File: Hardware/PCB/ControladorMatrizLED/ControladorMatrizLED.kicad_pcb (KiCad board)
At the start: 2 copper layers, 18 parts

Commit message: Avance sobre Esquematico y PCB - Pistas terminadas
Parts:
- moved C2_OUT1 51.8 mm to (135.6, 78.2), turned to 270 degrees
- moved C1_OUT1 47.2 mm to (112.3, 124.5), turned to 90 degrees
- moved C3_OUT1 27.7 mm to (108.0, 78.2)
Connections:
- C1_OUT1 pad 1: /C1_QA -> C1_QA
- C1_OUT1 pad 2: /C1_QB -> C1_QB
- C1_OUT1 pad 3: /C1_QC -> C1_QC
- C1_OUT1 pad 4: /C1_QD -> C1_QD
- C1_OUT1 pad 5: /C1_QE -> C1_QE
- C1_OUT1 pad 6: /C1_QF -> C1_QF
- C1_OUT1 pad 7: /C1_QG -> C1_QG
- C1_OUT1 pad 8: /C1_QH -> C1_QH
- C2_OUT1 pad 1: /C2_QA -> C2_QA
- C2_OUT1 pad 2: /C2_QB -> C2_QB
- C2_OUT1 pad 3: /C2_QC -> C2_QC
- C2_OUT1 pad 4: /C2_QD -> C2_QD
- C2_OUT1 pad 5: /C2_QE -> C2_QE
- C2_OUT1 pad 6: /C2_QF -> C2_QF
- C2_OUT1 pad 7: /C2_QG -> C2_QG
- C2_OUT1 pad 8: /C2_QH -> C2_QH
- C3_OUT1 pad 1: /C3_QA -> C3_QA
- C3_OUT1 pad 2: /C3_QB -> C3_QB
- C3_OUT1 pad 3: /C3_QC -> C3_QC
- C3_OUT1 pad 4: /C3_QD -> C3_QD
- C3_OUT1 pad 5: /C3_QE -> C3_QE
- C3_OUT1 pad 6: /C3_QF -> C3_QF
- C3_OUT1 pad 7: /C3_QG -> C3_QG
- C3_OUT1 pad 8: /C3_QH -> C3_QH
- EXP_C1 pad 1: /C3_SD -> C3_SD
- EXP_C1 pad 2: /C3_CLK -> C3_CLK
- EXP_C1 pad 3: /C3_LATCH -> C3_LATCH
- EXP_F1 pad 1: /F1_SD -> F1_SD
- EXP_F1 pad 2: /F1_CLK -> F1_CLK
- EXP_F1 pad 3: /F1_LATCH -> C3_LATCH
- F1_OUT1 pad 1: /F1_QA -> F1_QA
- F1_OUT1 pad 2: /F1_QB -> F1_QB
- F1_OUT1 pad 3: /F1_QC -> F1_QC
- F1_OUT1 pad 4: /F1_QD -> F1_QD
- F1_OUT1 pad 5: /F1_QE -> F1_QE
- F1_OUT1 pad 6: /F1_QF -> F1_QF
- F1_OUT1 pad 7: /F1_QG -> F1_QG
- F1_OUT1 pad 8: /F1_QH -> F1_QH
- J_MODE_CLK1 pad 1: /CMLED/GPIO3 -> F1_CLK
- J_MODE_CLK1 pad 3: /CMLED/GPIO8 -> C3_CLK
- J_MODE_SD1 pad 1: /CMLED/JF_OUT -> F1_SD
- REGC1 pad 1: /CMLED/C1_QB -> C1_QB
- REGC1 pad 11: /CMLED/GPIO8 -> C3_CLK
- REGC1 pad 12: /CMLED/GPIO5 -> C3_LATCH
- REGC1 pad 15: /CMLED/C1_QA -> C1_QA
- REGC1 pad 2: /CMLED/C1_QC -> C1_QC
- REGC1 pad 3: /CMLED/C1_QD -> C1_QD
- REGC1 pad 4: /CMLED/C1_QE -> C1_QE
- REGC1 pad 5: /CMLED/C1_QF -> C1_QF
- REGC1 pad 6: /CMLED/C1_QG -> C1_QG
- REGC1 pad 7: /CMLED/C1_QH -> C1_QH
- REGC2 pad 1: /CMLED/C2_QB -> C2_QB
- REGC2 pad 11: /CMLED/GPIO8 -> C3_CLK
- REGC2 pad 12: /CMLED/GPIO5 -> C3_LATCH
- REGC2 pad 15: /CMLED/C2_QA -> C2_QA
- REGC2 pad 2: /CMLED/C2_QC -> C2_QC
- REGC2 pad 3: /CMLED/C2_QD -> C2_QD
- REGC2 pad 4: /CMLED/C2_QE -> C2_QE
- REGC2 pad 5: /CMLED/C2_QF -> C2_QF
- REGC2 pad 6: /CMLED/C2_QG -> C2_QG
- REGC2 pad 7: /CMLED/C2_QH -> C2_QH
- REGC3 pad 1: /CMLED/C3_QB -> C3_QB
- REGC3 pad 12: /CMLED/GPIO5 -> C3_LATCH
- REGC3 pad 15: /CMLED/C3_QA -> C3_QA
- REGC3 pad 2: /CMLED/C3_QC -> C3_QC
- REGC3 pad 3: /CMLED/C3_QD -> C3_QD
- REGC3 pad 4: /CMLED/C3_QE -> C3_QE
- REGC3 pad 5: /CMLED/C3_QF -> C3_QF
- REGC3 pad 6: /CMLED/C3_QG -> C3_QG
- REGC3 pad 7: /CMLED/C3_QH -> C3_QH
- REGC3 pad 9: /CMLED/C3_SD -> C3_SD
- REGF1 pad 1: /CMLED/F1_QB -> F1_QB
- REGF1 pad 11: /CMLED/GPIO3 -> F1_CLK
- REGF1 pad 12: /CMLED/GPIO5 -> C3_LATCH
- REGF1 pad 15: /CMLED/F1_QA -> F1_QA
- REGF1 pad 2: /CMLED/F1_QC -> F1_QC
- REGF1 pad 3: /CMLED/F1_QD -> F1_QD
- REGF1 pad 4: /CMLED/F1_QE -> F1_QE
- REGF1 pad 5: /CMLED/F1_QF -> F1_QF
- REGF1 pad 6: /CMLED/F1_QG -> F1_QG
- REGF1 pad 7: /CMLED/F1_QH -> F1_QH
- REGF1 pad 9: /CMLED/JF_OUT -> F1_SD
- XA1 pad 74: /CMLED/GPIO3 -> F1_CLK
- XA1 pad 76: /CMLED/GPIO5 -> C3_LATCH
- XA1 pad 80: /CMLED/GPIO8 -> C3_CLK
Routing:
- net C3_LATCH: track 0.00 -> 168.8 mm
- net /CMLED/GPIO5: track 124.3 -> 0.00 mm
- net /CMLED/GPIO8: track 117.6 -> 0.00 mm
- net C3_CLK: track 0.00 -> 109.4 mm
- net F1_CLK: track 0.00 -> 67.8 mm
- net C3_SD: track 0.00 -> 66.2 mm
- net /CMLED/GPIO3: track 58.9 -> 0.00 mm
- net F1_SD: track 0.00 -> 42.5 mm
- net C3_QA: track 0.00 -> 17.6 mm
- net C2_QA: track 0.00 -> 17.2 mm
- net /CMLED/JF_OUT: track 16.9 -> 0.00 mm
- net F1_QA: track 0.00 -> 15.2 mm
- net C1_QA: track 0.00 -> 15.2 mm
- net C3_QH: track 0.00 -> 6.86 mm
- net C3_QG: track 0.00 -> 6.86 mm
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
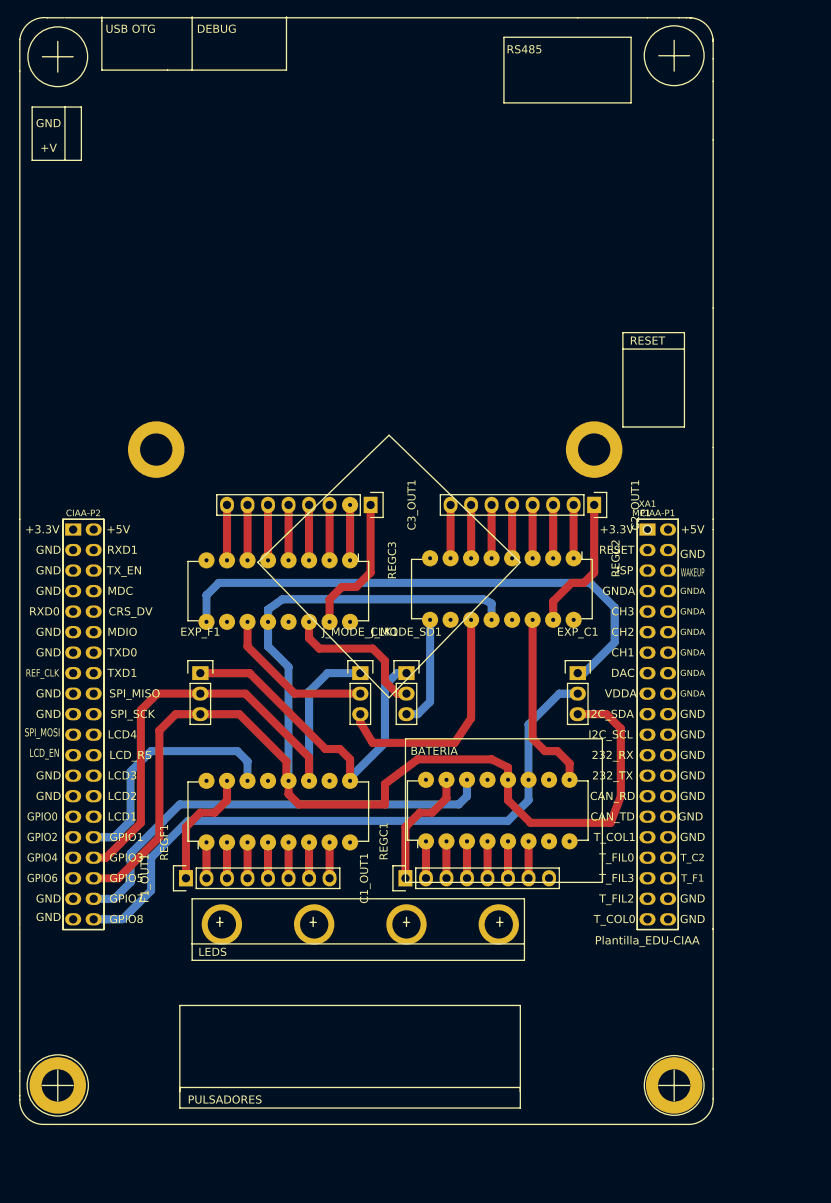
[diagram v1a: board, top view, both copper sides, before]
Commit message: Pistas completas y prueba de impreso añadida
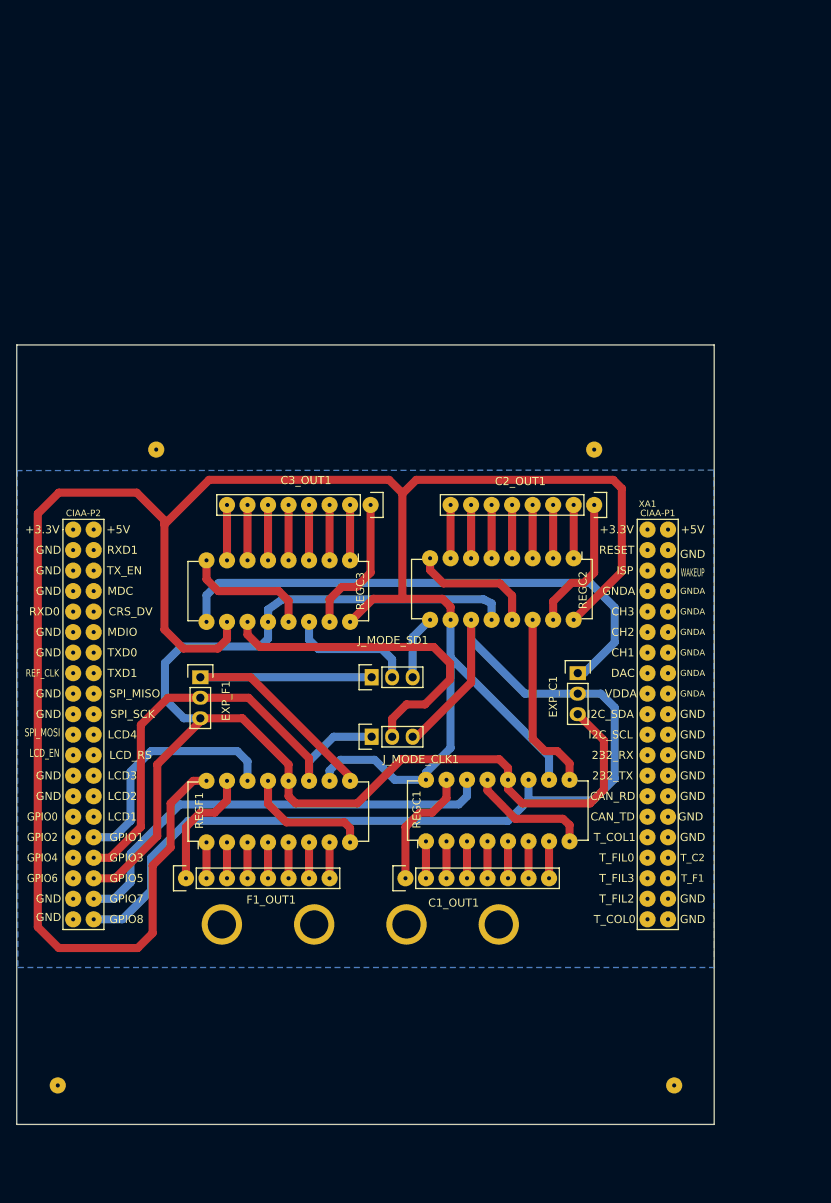
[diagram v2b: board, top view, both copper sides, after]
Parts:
- removed MP1: Plantilla_EDU-CIAA, Poncho_Esqueleto:Plantilla_EDU-CIAA
- moved J_MODE_CLK1 8.00 mm to (108.1, 106.9), turned to 90 degrees
- moved J_MODE_SD1 4.35 mm to (108.1, 99.6), turned to 90 degrees
- moved EXP_F1 0.51 mm to (86.9, 99.6)
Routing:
- net VCC: track 0.00 -> 297.7 mm
- net GND: track 0.00 -> 63.5 mm
- net /CMLED/JCLK_C3: track 19.4 -> 41.5 mm
- net C3_CLK: track 109.4 -> 127.0 mm
- net F1_CLK: track 67.8 -> 59.6 mm
- net C3_LATCH: track 168.8 -> 161.3 mm
- net /CMLED/JC2_OUT: track 13.7 -> 8.01 mm
- net C1_QH: track 0.00 -> 4.57 mm
- net F1_SD: track 42.5 -> 45.7 mm
- net /CMLED/JC3_OUT: track 18.4 -> 15.7 mm
- added copper zone on B.Cu, net GND
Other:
- board outline added: 86.4 x 96.5 mm

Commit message: Actualizacion con modelo poncho grande y LCD
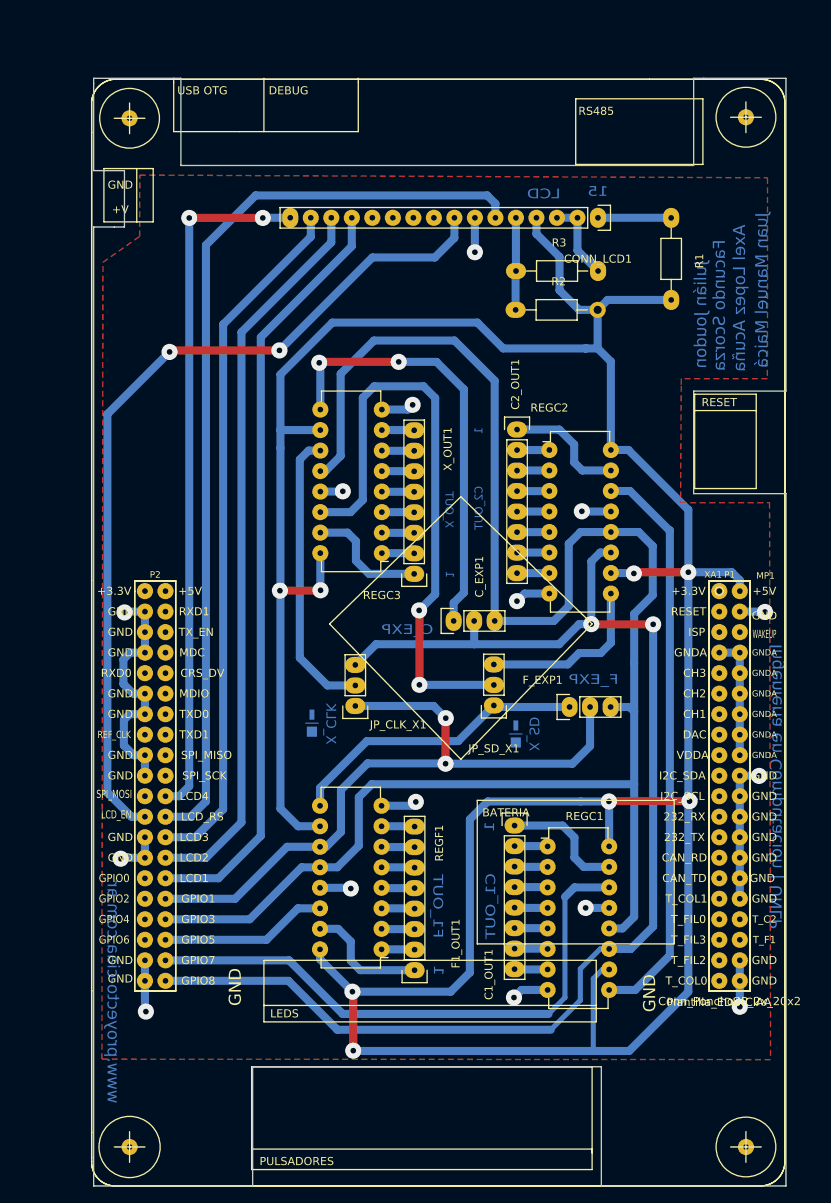
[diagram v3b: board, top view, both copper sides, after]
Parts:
- removed C3_OUT1: CONN_01X08, Pin_Headers:Pin_Header_Straight_1x08
- removed EXP_C1, EXP_F1, J_MODE_CLK1, J_MODE_SD1: CONN_01X03, Pin_Headers:Pin_Header_Straight_1x03
- removed H1, H2, H3, H4: PCB_HOLE, Poncho_Modelos:Led_Hole
- added CONN_LCD1: CONN_01X16, Socket_Strips:Socket_Strip_Straight_1x16, F.Cu at (136.1, 42.7)
- added C_EXP1: CONN_01X03, Socket_Strips:Socket_Strip_Straight_1x03, F.Cu at (118.2, 92.6)
- added F_EXP1: CONN_01X03, Socket_Strips:Socket_Strip_Straight_1x03, F.Cu at (132.6, 103.3)
- added JP_CLK_X1: CONN_01X03, Socket_Strips:Socket_Strip_Straight_1x03, F.Cu at (106.1, 103.1)
- added JP_SD_X1: CONN_01X03, Socket_Strips:Socket_Strip_Straight_1x03, F.Cu at (123.2, 103.1)
- added MP1: Plantilla_EDU-CIAA, Poncho_Esqueleto:Plantilla_EDU-CIAA, F.Cu at (151.1, 88.9)
- added R1: R, Resistors_ThroughHole:Resistor_Horizontal_RM10mm, F.Cu at (145.2, 47.8)
- added R2: R, Resistors_ThroughHole:Resistor_Horizontal_RM10mm, F.Cu at (131.0, 54.1)
- added R3: R, Resistors_ThroughHole:Resistor_Horizontal_RM10mm, F.Cu at (131.0, 49.3)
- added X_OUT1: CONN_01X08, Socket_Strips:Socket_Strip_Straight_1x08, F.Cu at (113.3, 86.8)
- C1_OUT1, C2_OUT1, F1_OUT1: footprint Pin_Headers:Pin_Header_Straight_1x08 -> Socket_Strips:Socket_Strip_Straight_1x08
- XA1: value Conn_PonchoMP_2x_20x2 -> Conn_Poncho2P_2x_20x2; footprint Poncho_Esqueleto:Conn_Poncho_Mediano -> mod:poncho_grande
- moved F1_OUT1 30.5 mm to (113.4, 135.8)
- moved REGF1 25.4 mm to (109.3, 133.3), turned to 180 degrees
- moved REGC1 15.1 mm to (129.9, 120.5), turned to 0 degrees
- moved C1_OUT1 15.0 mm to (125.8, 117.9), turned to 270 degrees
- moved REGC2 13.7 mm to (130.1, 71.4), turned to 0 degrees
- moved C2_OUT1 13.4 mm to (126.1, 68.9)
- moved XA1 11.7 mm to (151.1, 88.9)
- moved REGC3 4.04 mm to (109.3, 84.2), turned to 180 degrees
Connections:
- net /CMLED/GPIO7 renamed /Circuito Principal/GPIO7
- net C1_QA renamed Net-(C1_OUT1-Pad1)
- net C1_QB renamed Net-(C1_OUT1-Pad2)
- net C1_QC renamed Net-(C1_OUT1-Pad3)
- net C1_QD renamed Net-(C1_OUT1-Pad4)
- net C1_QE renamed Net-(C1_OUT1-Pad5)
- net C1_QF renamed Net-(C1_OUT1-Pad6)
- net C1_QG renamed Net-(C1_OUT1-Pad7)
- net C1_QH renamed Net-(C1_OUT1-Pad8)
- net C2_QA renamed Net-(C2_OUT1-Pad1)
- net C2_QB renamed Net-(C2_OUT1-Pad2)
- net C2_QC renamed Net-(C2_OUT1-Pad3)
- net C2_QD renamed Net-(C2_OUT1-Pad4)
- net C2_QE renamed Net-(C2_OUT1-Pad5)
- net C2_QF renamed Net-(C2_OUT1-Pad6)
- net C2_QG renamed Net-(C2_OUT1-Pad7)
- net C2_QH renamed Net-(C2_OUT1-Pad8)
- net C3_CLK renamed /Circuito Principal/GPIO8
- net F1_QA renamed Net-(F1_OUT1-Pad1)
- net F1_QB renamed Net-(F1_OUT1-Pad2)
- net F1_QC renamed Net-(F1_OUT1-Pad3)
- net F1_QD renamed Net-(F1_OUT1-Pad4)
- net F1_QE renamed Net-(F1_OUT1-Pad5)
- net F1_QF renamed Net-(F1_OUT1-Pad6)
- net F1_QG renamed Net-(F1_OUT1-Pad7)
- net F1_QH renamed Net-(F1_OUT1-Pad8)
- net Net-(XA1-Pad69) renamed /Conector del Poncho/GPIO0
- net Net-(XA1-Pad71) renamed /Conector del Poncho/GPIO2
- net Net-(XA1-Pad73) renamed /Conector del Poncho/GPIO4
- net Net-(XA1-Pad75) renamed /Conector del Poncho/GPIO6
- REGC1 pad 12: C3_LATCH -> /Circuito Principal/GPIO3
- REGC2 pad 12: C3_LATCH -> /Circuito Principal/GPIO3
- REGC2 pad 9: /CMLED/JC2_OUT -> Net-(JP_SD_X1-Pad3)
- REGC3 pad 1: C3_QB -> Net-(REGC3-Pad1)
- REGC3 pad 11: /CMLED/JCLK_C3 -> Net-(JP_CLK_X1-Pad2)
- REGC3 pad 12: C3_LATCH -> /Circuito Principal/GPIO3
- REGC3 pad 14: /CMLED/JC3_OUT -> Net-(JP_SD_X1-Pad2)
- REGC3 pad 15: C3_QA -> Net-(REGC3-Pad15)
- REGC3 pad 2: C3_QC -> Net-(REGC3-Pad2)
- REGC3 pad 3: C3_QD -> Net-(REGC3-Pad3)
- REGC3 pad 4: C3_QE -> Net-(REGC3-Pad4)
- REGC3 pad 5: C3_QF -> Net-(REGC3-Pad5)
- REGC3 pad 6: C3_QG -> Net-(REGC3-Pad6)
- REGC3 pad 7: C3_QH -> Net-(REGC3-Pad7)
- REGC3 pad 9: C3_SD -> Net-(C_EXP1-Pad1)
- REGF1 pad 11: F1_CLK -> /Circuito Principal/GPIO1
- REGF1 pad 12: C3_LATCH -> /Circuito Principal/GPIO3
- REGF1 pad 14: /CMLED/GPIO1 -> /Circuito Principal/GPIO5
- REGF1 pad 9: F1_SD -> Net-(F_EXP1-Pad1)
- XA1 pad 1: (no net) -> +3.3V
- XA1 pad 10: (no net) -> GNDA
- XA1 pad 11: (no net) -> /Conector del Poncho/ADC2
- XA1 pad 12: (no net) -> GNDA
- XA1 pad 13: (no net) -> /Conector del Poncho/ADC1
- XA1 pad 14: (no net) -> GNDA
- XA1 pad 15: (no net) -> /Conector del Poncho/DAC
- XA1 pad 16: (no net) -> GNDA
- XA1 pad 17: (no net) -> +3.3VADC
- XA1 pad 18: (no net) -> GNDA
- XA1 pad 19: (no net) -> /Conector del Poncho/SDA
- XA1 pad 2: (no net) -> VCC
- XA1 pad 20: (no net) -> GND
- XA1 pad 21: (no net) -> /Conector del Poncho/SCL
- XA1 pad 22: (no net) -> GND
- XA1 pad 23: (no net) -> /Conector del Poncho/RXD
- XA1 pad 24: (no net) -> GND
- XA1 pad 25: (no net) -> /Conector del Poncho/TXD
- XA1 pad 26: (no net) -> GND
- XA1 pad 27: (no net) -> /Conector del Poncho/RD
- XA1 pad 28: (no net) -> GND
- XA1 pad 29: (no net) -> /Conector del Poncho/TD
- XA1 pad 3: (no net) -> /Conector del Poncho/RESET
- XA1 pad 30: (no net) -> GND
- XA1 pad 31: (no net) -> /Conector del Poncho/COL1
- XA1 pad 32: (no net) -> GND
- XA1 pad 33: (no net) -> /Conector del Poncho/F0
- XA1 pad 34: (no net) -> /Conector del Poncho/COL2
- XA1 pad 35: (no net) -> /Conector del Poncho/F3
- XA1 pad 36: (no net) -> /Conector del Poncho/F1
- XA1 pad 37: (no net) -> /Conector del Poncho/F2
- XA1 pad 38: (no net) -> GND
- XA1 pad 39: (no net) -> /Conector del Poncho/COL0
- XA1 pad 4: (no net) -> GND
- XA1 pad 40: (no net) -> GND
- XA1 pad 41: (no net) -> +3.3VP
- XA1 pad 42: (no net) -> +5VP
- XA1 pad 43: (no net) -> GND
- XA1 pad 44: (no net) -> /Conector del Poncho/RXD1
- XA1 pad 45: (no net) -> GND
- XA1 pad 46: (no net) -> /Conector del Poncho/TXEN
- XA1 pad 47: (no net) -> GND
- XA1 pad 48: (no net) -> /Conector del Poncho/MDC
- XA1 pad 49: (no net) -> /Conector del Poncho/RXD0
- XA1 pad 5: (no net) -> /Conector del Poncho/ISP
- XA1 pad 50: (no net) -> /Conector del Poncho/CRS
- XA1 pad 51: (no net) -> GND
- XA1 pad 52: (no net) -> /Conector del Poncho/MDIO
- XA1 pad 53: (no net) -> GND
- XA1 pad 54: (no net) -> /Conector del Poncho/TXD0
- XA1 pad 55: (no net) -> /Conector del Poncho/RCLK
- XA1 pad 56: (no net) -> /Conector del Poncho/TXD1
- XA1 pad 57: (no net) -> GND
- XA1 pad 58: (no net) -> /Conector del Poncho/MISO
- XA1 pad 59: (no net) -> GND
- XA1 pad 6: (no net) -> /Conector del Poncho/WAKEUP
- XA1 pad 60: (no net) -> /Conector del Poncho/spiSCK
- XA1 pad 61: (no net) -> /Conector del Poncho/MOSI
- XA1 pad 62: (no net) -> /Circuito Principal/LCD4
- XA1 pad 63: (no net) -> /Circuito Principal/LCD_EN
- XA1 pad 64: (no net) -> /Circuito Principal/RS
- XA1 pad 65: (no net) -> GND
- XA1 pad 66: (no net) -> /Circuito Principal/LCD3
- XA1 pad 67: (no net) -> GND
- XA1 pad 68: (no net) -> /Circuito Principal/LCD2
- XA1 pad 7: (no net) -> GNDA
- XA1 pad 70: (no net) -> /Circuito Principal/LCD1
- XA1 pad 72: /CMLED/GPIO1 -> /Circuito Principal/GPIO1
- XA1 pad 74: F1_CLK -> /Circuito Principal/GPIO3
- XA1 pad 76: C3_LATCH -> /Circuito Principal/GPIO5
- XA1 pad 77: (no net) -> GND
- XA1 pad 79: (no net) -> GND
- XA1 pad 8: (no net) -> GNDA
- XA1 pad 9: (no net) -> /Conector del Poncho/ADC3
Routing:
- net /Circuito Principal/GPIO3: track 0.00 -> 217.6 mm
- net C3_LATCH: track 161.3 -> 0.00 mm
- net /Circuito Principal/RS: track 0.00 -> 115.2 mm
- net /Circuito Principal/LCD_EN: track 0.00 -> 107.3 mm, vias 0 -> 2
- net /Circuito Principal/LCD1: track 0.00 -> 95.2 mm
- net VCC: track 297.7 -> 389.9 mm, vias 0 -> 8
- net /Circuito Principal/LCD2: track 0.00 -> 90.7 mm
- net /Circuito Principal/LCD4: track 0.00 -> 86.3 mm, vias 0 -> 2
- net /Circuito Principal/LCD3: track 0.00 -> 86.3 mm
- net /Circuito Principal/GPIO1: track 0.00 -> 85.8 mm, vias 0 -> 2
- net Net-(JP_SD_X1-Pad2): track 0.00 -> 74.3 mm, vias 0 -> 2
- net C3_SD: track 66.2 -> 0.00 mm
- net F1_CLK: track 59.6 -> 0.00 mm
- net Net-(C_EXP1-Pad1): track 0.00 -> 54.4 mm, vias 0 -> 2
- net GND: track 63.5 -> 114.9 mm, vias 0 -> 15
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- added copper zone on F.Cu, net GND
- removed copper zone on B.Cu, net GND
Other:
- board size 86.4 x 96.5 mm -> 85.7 x 137.2 mm
- net class Default: via_dia 0.6 -> 2; via_drill 0.4 -> 0.7
- board text added: "1"
- board text added: "14----------------1-16-15"
- board text added: "15"
- board text added: "Axel Lopez Acuña"
- board text added: "C1_OUT"
- board text added: "C2_OUT"
- board text added: "C_EXP"
- board text added: "Colocar código de Poncho en cobre, serigrafía y rótulo."
- board text added: "F1_OUT"
- board text added: "F_EXP"
- board text added: "Facundo Scorza"
- board text added: "GND"
- board text added: "Ingeniería en Computación | UNLP"
- board text added: "Juan Manuel Maicá"
- board text added: "Julián Joudon"
- board text added: "LCD"
- board text added: "PONCHO GRANDE http://www.proyecto-ciaa.com.ar/"
- board text added: "STACK-UP PCB de simple faz Sin requisitos de Stackup"
- board text added: "X_CLK"
- board text added: "X_OUT"
- board text added: "X_SD"
- board text added: "www.proyecto-ciaa.com.ar"
- board text added: "■|▬"
- board text removed: "Diseño simple faz. Sin requerimientos especiales."
- board text removed: "PONCHO MEDIANO http://www.proyecto-ciaa.com.ar/"
- board text removed: "STACK-UP"
- board text removed: "Se sugiere colocar código de Poncho en cobre, serigrafía y rótulo."
